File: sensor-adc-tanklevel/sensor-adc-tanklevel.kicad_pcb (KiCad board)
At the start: 2 copper layers, 40 x 19.4 mm, 13 parts, among them J2 ESP-01S, U1 LMZM23601V3SILR, U2 ADS1115

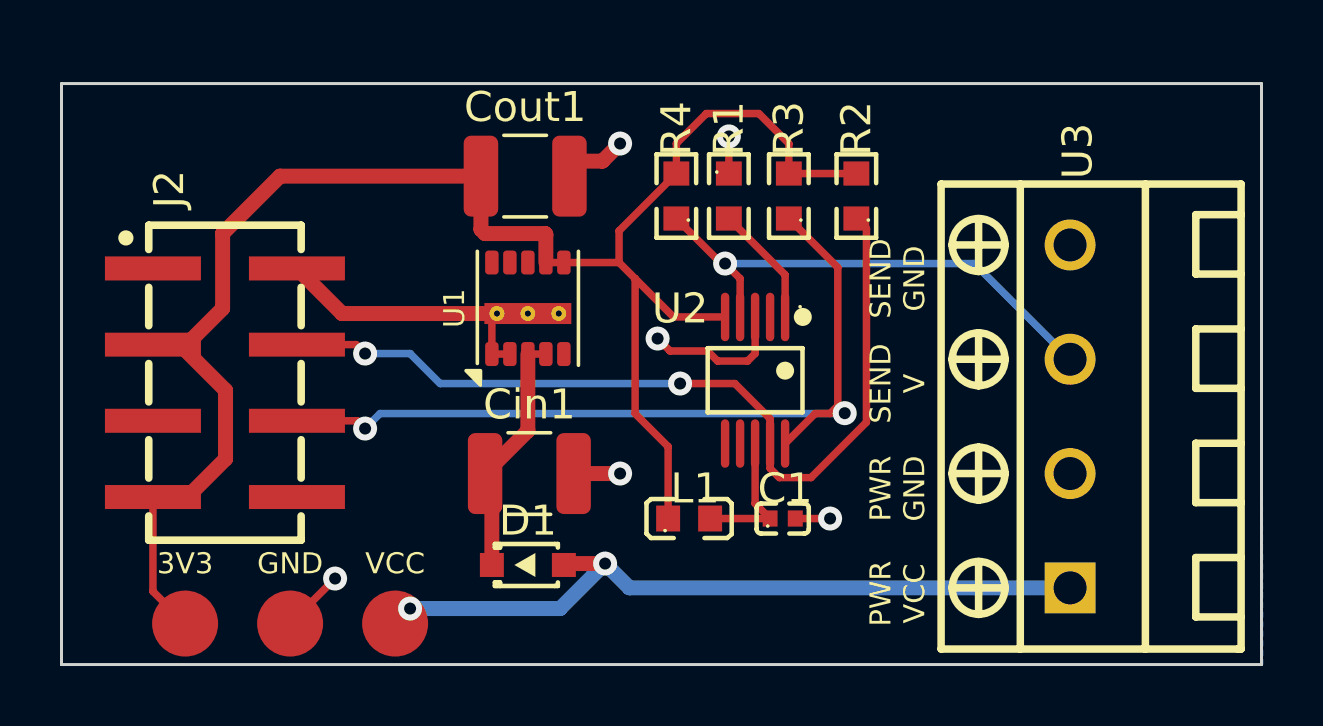
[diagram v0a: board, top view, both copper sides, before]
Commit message: Replaced LMZM23601V3SILR with AP63203WU-7
It turned out that the price of the TI LMZM23601V3SILR. Replaced
this with cheaper one. I hope it works...
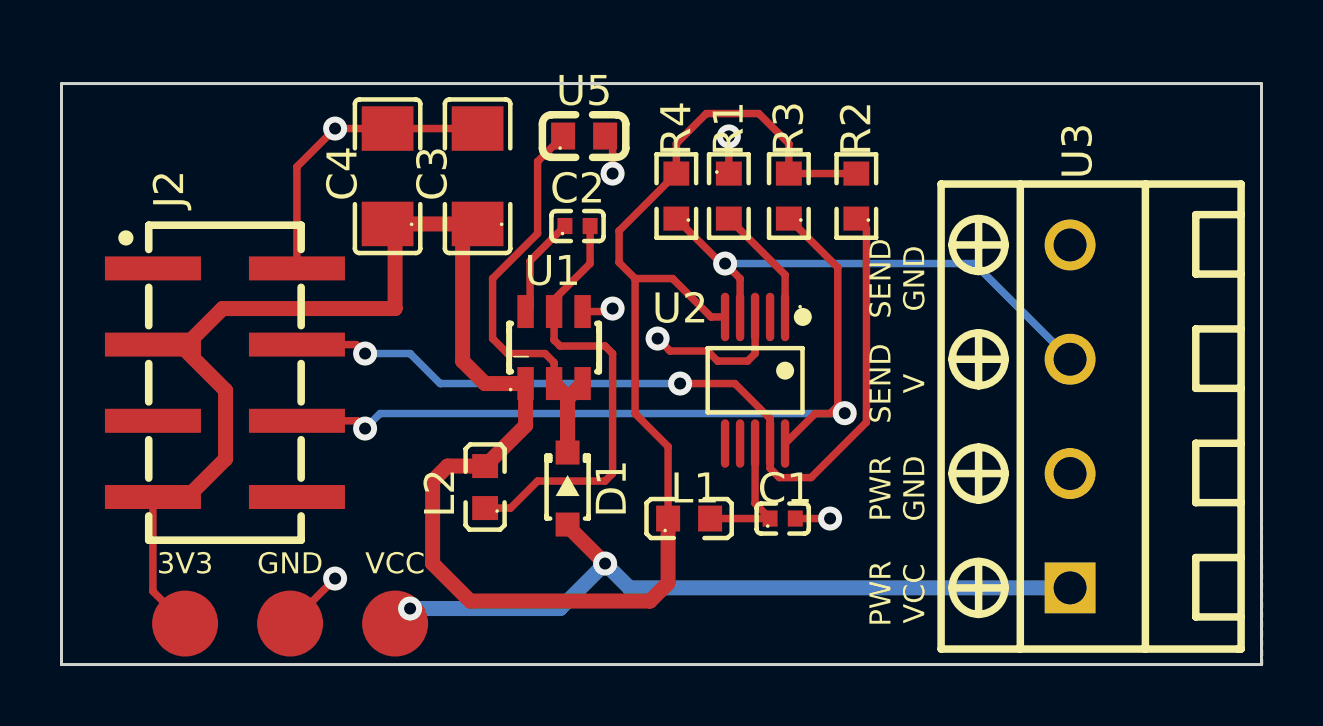
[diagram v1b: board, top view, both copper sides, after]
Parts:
- removed Cin1: 10μF (50V), Capacitor_SMD:C_1210_3225Metric
- removed Cout1: 33μF (6.3V), Capacitor_SMD:C_1210_3225Metric
- added C2: 100nF, lcsc_footprints:C1525_C0402, F.Cu at (129.1, 88.2)
- added C3: 22uF, lcsc_footprints:C12891_C1206, F.Cu at (125.8, 86.6)
- added C4: 22uF, lcsc_footprints:C12891_C1206, F.Cu at (122.8, 86.6)
- added L2: 3.9uH, lcsc_footprints:C57836_L0603, F.Cu at (126.0, 97.0)
- added U5: 10 µF, lcsc_footprints:C22367827_C0603, F.Cu at (129.3, 85.2)
- U1: value LMZM23601V3SILR -> AP63203WU-7; footprint Package_LGA:Texas_SIL0010A_MicroSiP-10-1EP_3.8x3mm_P0.6mm_EP0.7x2.9mm_ThermalVias -> lcsc_footprints:C780769_TSOT-26_L2_9-W1_6-P0_95-LS2_8-BL
- moved D1 2.87 mm to (128.8, 97.0), turned to -90 degrees
- moved U1 1.57 mm to (128.3, 92.3), turned to 0 degrees
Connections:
- U1 pad 1: Earth -> +3V3
- U1 pad 2: Earth -> Net-(D1-K)
- U1 pad 4: Net-(D1-K) -> Earth
- U1 pad 5: unconnected-(U1-PG-Pad5) -> Net-(U1-SW)
- U1 pad 6: +3V3 -> Net-(U1-BST)
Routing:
- net +3V3: track 60.4 -> 78.7 mm
- net Net-(U1-SW): track 0.00 -> 15.2 mm
- net Net-(D1-K): track 8.32 -> 15.8 mm
- net Net-(U1-BST): track 0.00 -> 3.39 mm
- net Earth: track 23.2 -> 22.2 mm, vias 6 -> 7

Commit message: Changed all symbols and footprints to LCSC versions
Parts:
- CN2: renamed from J2; value ESP-01S -> PM254-2-04-S-8.5; footprint C3975149:HDR-SMD_8P-P2.54-V-F-R2-C4-S7.1 -> lcsc_footprints:C3975149_HDR-SMD_8P-P2_54-V-F-R2-C4-S7_1
- D1: value D -> S7116-300A; footprint C5174649:SOD-323_L1.7-W1.3-LS2.5-RD -> lcsc_footprints:C5174649_SOD-323_L1_7-W1_3-LS2_5-RD
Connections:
- CN2 pad 1: Earth -> unconnected-(CN2-Pad1)
- CN2 pad 2: unconnected-(J2-TX-Pad2) -> Earth
- CN2 pad 3: /SDA -> +3V3
- CN2 pad 4: +3V3 -> /SDA
- CN2 pad 5: /SCL -> unconnected-(CN2-Pad5)
- CN2 pad 6: unconnected-(J2-Pad6) -> /SCL
- CN2 pad 7: unconnected-(J2-RX-Pad7) -> +3V3
- CN2 pad 8: +3V3 -> unconnected-(CN2-Pad8)

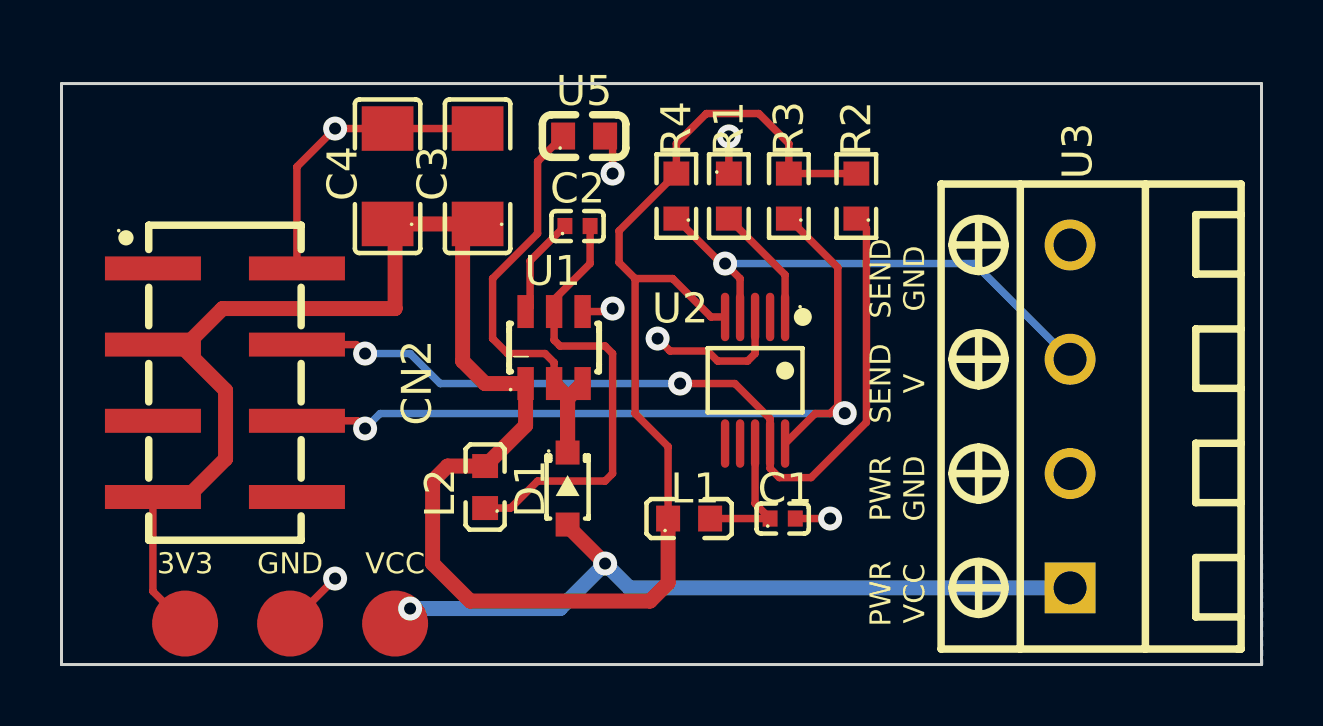
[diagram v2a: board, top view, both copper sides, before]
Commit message: Minor finishing touches before production
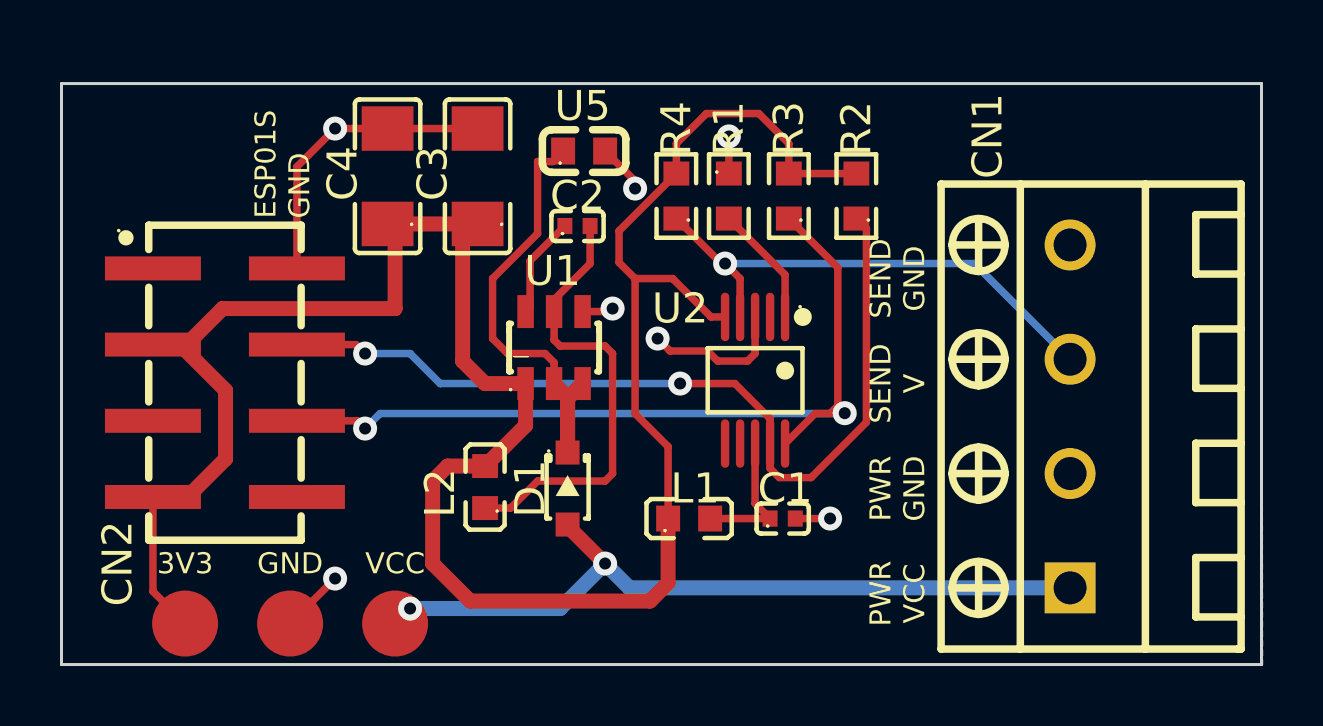
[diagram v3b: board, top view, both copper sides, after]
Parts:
- moved U5 0.50 mm to (129.3, 85.8)
- renumbered U3 to CN1
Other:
- board text added: "ESP01S GND"
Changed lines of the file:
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@@
 	(footprint "lcsc_footprints:C22367827_C0603"
 		(layer "F.Cu")
-		(at 129.3 85.25)
+		(at 129.3 85.75)
 		(property "Reference" "U5"
-			(at 0 -1.5 0)
+			(at -0.05 -1.5 0)
 			(layer "F.SilkS")
 			(effects
@@
 		(descr "100nF (104) ±10% 16V")
 		(property "Reference" "C2"
-			(at 0 -1.25 0)
+			(at 0 -1 0)
 			(layer "F.SilkS")
 			(effects
@@
 		(at 117.328 93.472 -90)
 		(property "Reference" "CN2"
-			(at 0 -6.4 90)
+			(at 6.028 3.578 90)
 			(layer "F.SilkS")
 			(effects
@@
 		)
 		(property "Value" "PM254-2-04-S-8.5"
-			(at 0 6.4 90)
+			(at 0.278 4.578 90)
 			(layer "F.Fab")
 			(effects
@@
 		(layer "F.Cu")
 		(at 145.5 94.6 90)
-		(property "Reference" "U3"
-			(at 8.85 0.25 90)
+		(property "Reference" "CN1"
+			(at 9.35 -2.75 90)
 			(layer "F.SilkS")
 			(effects
@@
 		)
 	)
+	(gr_text "ESP01S\nGND"
+		(at 119.25 88 90)
+		(layer "F.SilkS")
+		(effects
+			(font
+				(size 0.7 0.7)
+				(thickness 0.15)
+			)
+			(justify left)
+		)
+	)
 	(gr_text "SEND\nGND"
 		(at 139.75 90 90)
@@
 	)
 	(segment
-		(start 127.75 86.1)
-		(end 128.6 85.25)
-		(width 0.25)
-		(layer "F.Cu")
-		(net "Net-(D1-K)")
-	)
-	(segment
 		(start 127.75 88.5)
 		(end 127.75 86.1)
@@
 	)
 	(segment
+		(start 127.75 86.1)
+		(end 128.25 86.1)
+		(width 0.25)
+		(layer "F.Cu")
+		(net "Net-(D1-K)")
+	)
+	(segment
 		(start 128.75 95.8)
 		(end 128.75 94)
@@
 	)
 	(segment
+		(start 128.25 86.1)
+		(end 128.6 85.75)
+		(width 0.25)
+		(layer "F.Cu")
+		(net "Net-(D1-K)")
+	)
+	(segment
 		(start 126.25 90)
 		(end 127.75 88.5)
@@
 	)
 	(segment
-		(start 130.25 85.5)
-		(end 130.25 86.5)
+		(start 135 91.28)
+		(end 135 92.5)
 		(width 0.25)
 		(layer "F.Cu")
@@
 	)
 	(segment
-		(start 135 91.28)
-		(end 135 92.5)
+		(start 133.415 92.415)
+		(end 132.165 92.415)
 		(width 0.25)
 		(layer "F.Cu")
@@
 	)
 	(segment
-		(start 133.415 92.415)
-		(end 132.165 92.415)
+		(start 131 86.75)
+		(end 131 87)
 		(width 0.25)
 		(layer "F.Cu")
@@
 	)
 	(segment
+		(start 130 85.75)
+		(end 131 86.75)
+		(width 0.25)
+		(layer "F.Cu")
+		(net "Earth")
+	)
+	(segment
 		(start 129.25 91.1)
 		(end 129.25 90.682)
@@
 	)
 	(segment
-		(start 130 85.25)
-		(end 130.25 85.5)
-		(width 0.25)
-		(layer "F.Cu")
-		(net "Earth")
-	)
-	(segment
 		(start 130.15 91.1)
 		(end 130.25 91)
@@
 	)
 	(via
-		(at 130.25 86.5)
+		(at 131 87)
 		(size 0.8)
 		(drill 0.4)
@@
 	)
 	(group ""
-		(members "b307260c-7430-4ced-b89a-1bd0aa777e64" "dfa0b029-50de-4c42-8c1f-8f708cb93296")
+		(members "72f389a9-fddd-467f-ab5f-859006848ddf" "b307260c-7430-4ced-b89a-1bd0aa777e64"
+			"dfa0b029-50de-4c42-8c1f-8f708cb93296"
+		)
 	)
 	(group ""

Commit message: Changed L2 coil as the previous was not available
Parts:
- L2: value 3.9uH -> CMI160808U3R9KT; footprint lcsc_footprints:C57836_L0603 -> lcsc_footprints:C139210_L0603
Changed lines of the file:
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@@
 		)
 	)
-	(footprint "lcsc_footprints:C57836_L0603"
+	(footprint "lcsc_footprints:C139210_L0603"
 		(layer "F.Cu")
 		(at 126 96.95 90)
-		(descr "3.9uH")
 		(property "Reference" "L2"
-			(at -0.2 -1.5 90)
-			(layer "F.SilkS")
-			(effects
-				(font
-					(size 1 1)
-					(thickness 0.15)
-				)
-			)
-		)
-		(property "Value" "3.9uH"
+			(at 0 -4 90)
+			(layer "F.SilkS")
+			(effects
+				(font
+					(size 1 1)
+					(thickness 0.15)
+				)
+			)
+		)
+		(property "Value" "CMI160808U3R9KT"
 			(at 0 4 90)
 			(layer "F.Fab")
-			(hide yes)
-			(effects
-				(font
-					(size 1 1)
-					(thickness 0.15)
-				)
-			)
-		)
-		(property "Datasheet" "https://wmsc.lcsc.com/wmsc/upload/file/pdf/v2/lcsc/2310301641_Sunlord-SDFL1608Q3R9KTF_C57836.pdf"
+			(effects
+				(font
+					(size 1 1)
+					(thickness 0.15)
+				)
+			)
+		)
+		(property "Datasheet" "https://www.lcsc.com/datasheet/lcsc_datasheet_2302231230_FH--Guangdong-Fenghua-Advanced-Tech-CMI160808U3R9KT_C139210.pdf"
 			(at 0 0 90)
 			(layer "F.Fab")
@@
 			)
 		)
-		(property "Description" "3.9uH"
+		(property "Description" "CMI160808U3R9KT"
 			(at 0 0 90)
 			(layer "F.Fab")
@@
 			)
 		)
-		(property "LCSC" "C57836"
+		(property "LCSC Part" "C139210"
+			(at 0 0 90)
+			(layer "F.Fab")
+			(hide yes)
+			(effects
+				(font
+					(size 1.27 1.27)
+				)
+			)
+		)
+		(property "LCSC" "C139210"
 			(at 0 0 90)
 			(unlocked yes)
@@
 			)
 		)
-		(property "Manufacturer" "Sunlord(顺络)"
+		(property "Manufacturer" "FH(风华)"
 			(at 0 0 90)
 			(unlocked yes)
@@
 		)
 		(embedded_fonts no)
-		(model "${KIPRJMOD}/libs/lcsc/3dmodels/C57836.wrl"
+		(model "${KIPRJMOD}/libs/lcsc/3dmodels/C139210.wrl"
 			(offset
 				(xyz 1.6 -0.5 0)
